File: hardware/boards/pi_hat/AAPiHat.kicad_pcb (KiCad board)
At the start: 4 copper layers, 64.9 x 30 mm, 29 parts, among them J1 Raspberry_Pi_2_3, J2 Wurth RJ45, U1 RV1S9060A, U2 RV1S9060A, U3 MAX13487E, U4 ADP2303ARDZ

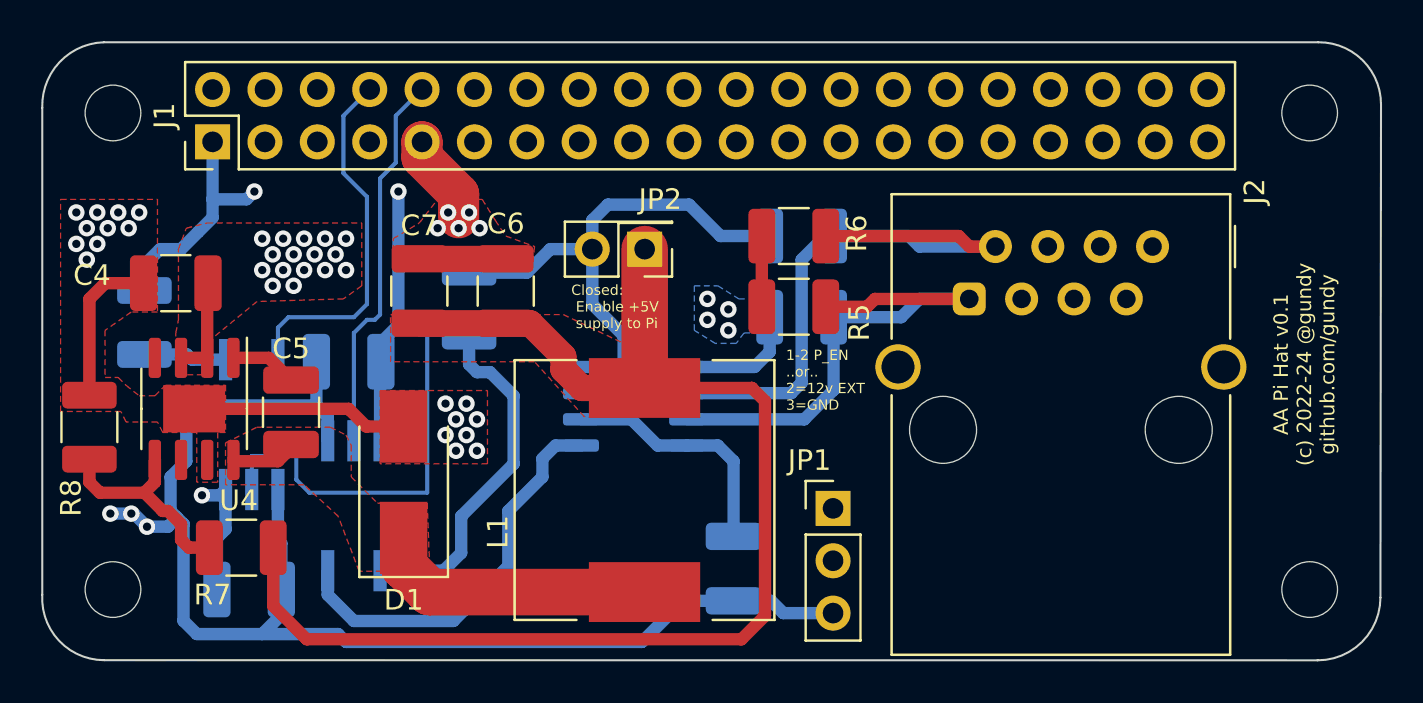
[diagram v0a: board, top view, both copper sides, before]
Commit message: Add schematics and board layout for RS485 interceptor module.
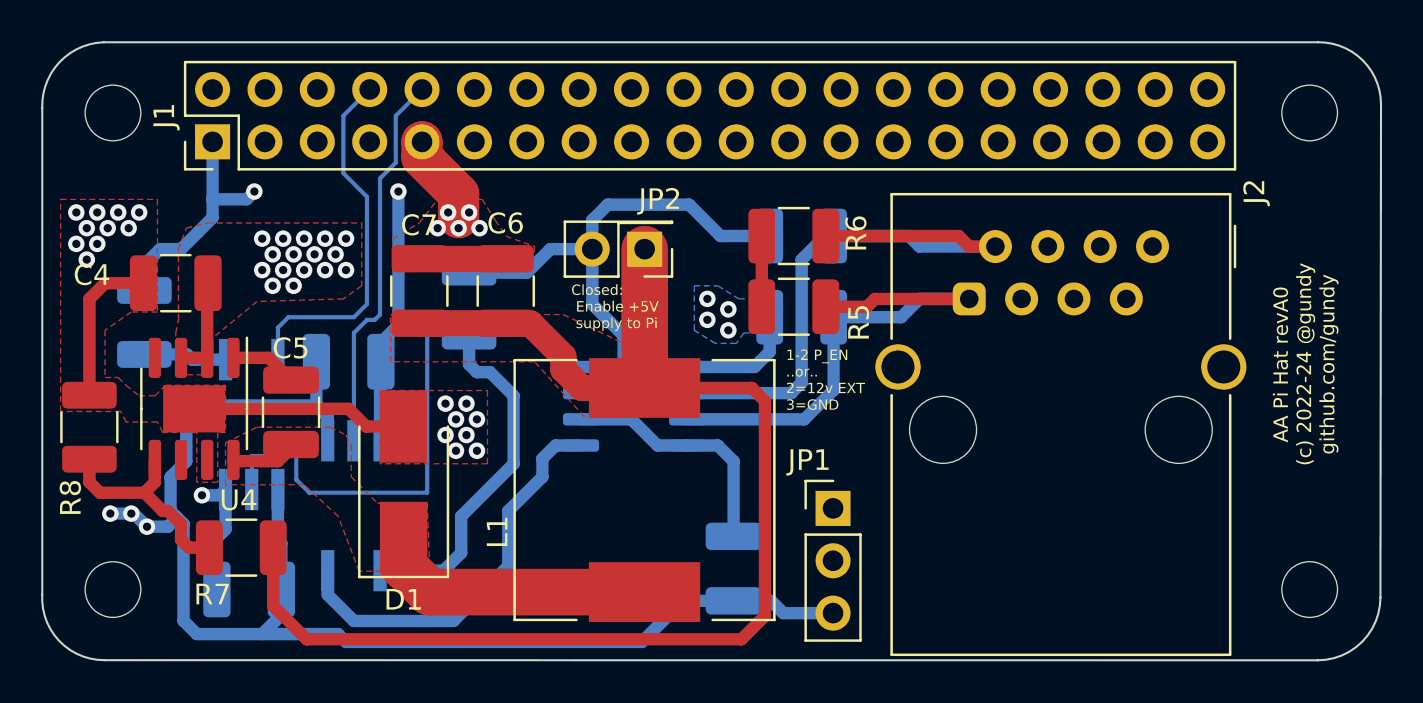
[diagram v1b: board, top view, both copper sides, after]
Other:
- board text added: "AA Pi Hat revA0 (c) 2022-24 @gundy github.com/gundy"
- board text removed: "AA Pi Hat v0.1 (c) 2022-24 @gundy github.com/gundy"
